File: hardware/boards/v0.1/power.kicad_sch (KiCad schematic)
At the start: 72 parts, among them IC3 SP3401-02UTG, J2 USB, U20 TPS62A02ADRLR, U23 FUSB302BxxMPX, U30 NTJD4401NT1G, U36 STM6601GU2BDM6F, U39 BQ27531YZFR-G1, U45 BQ24193

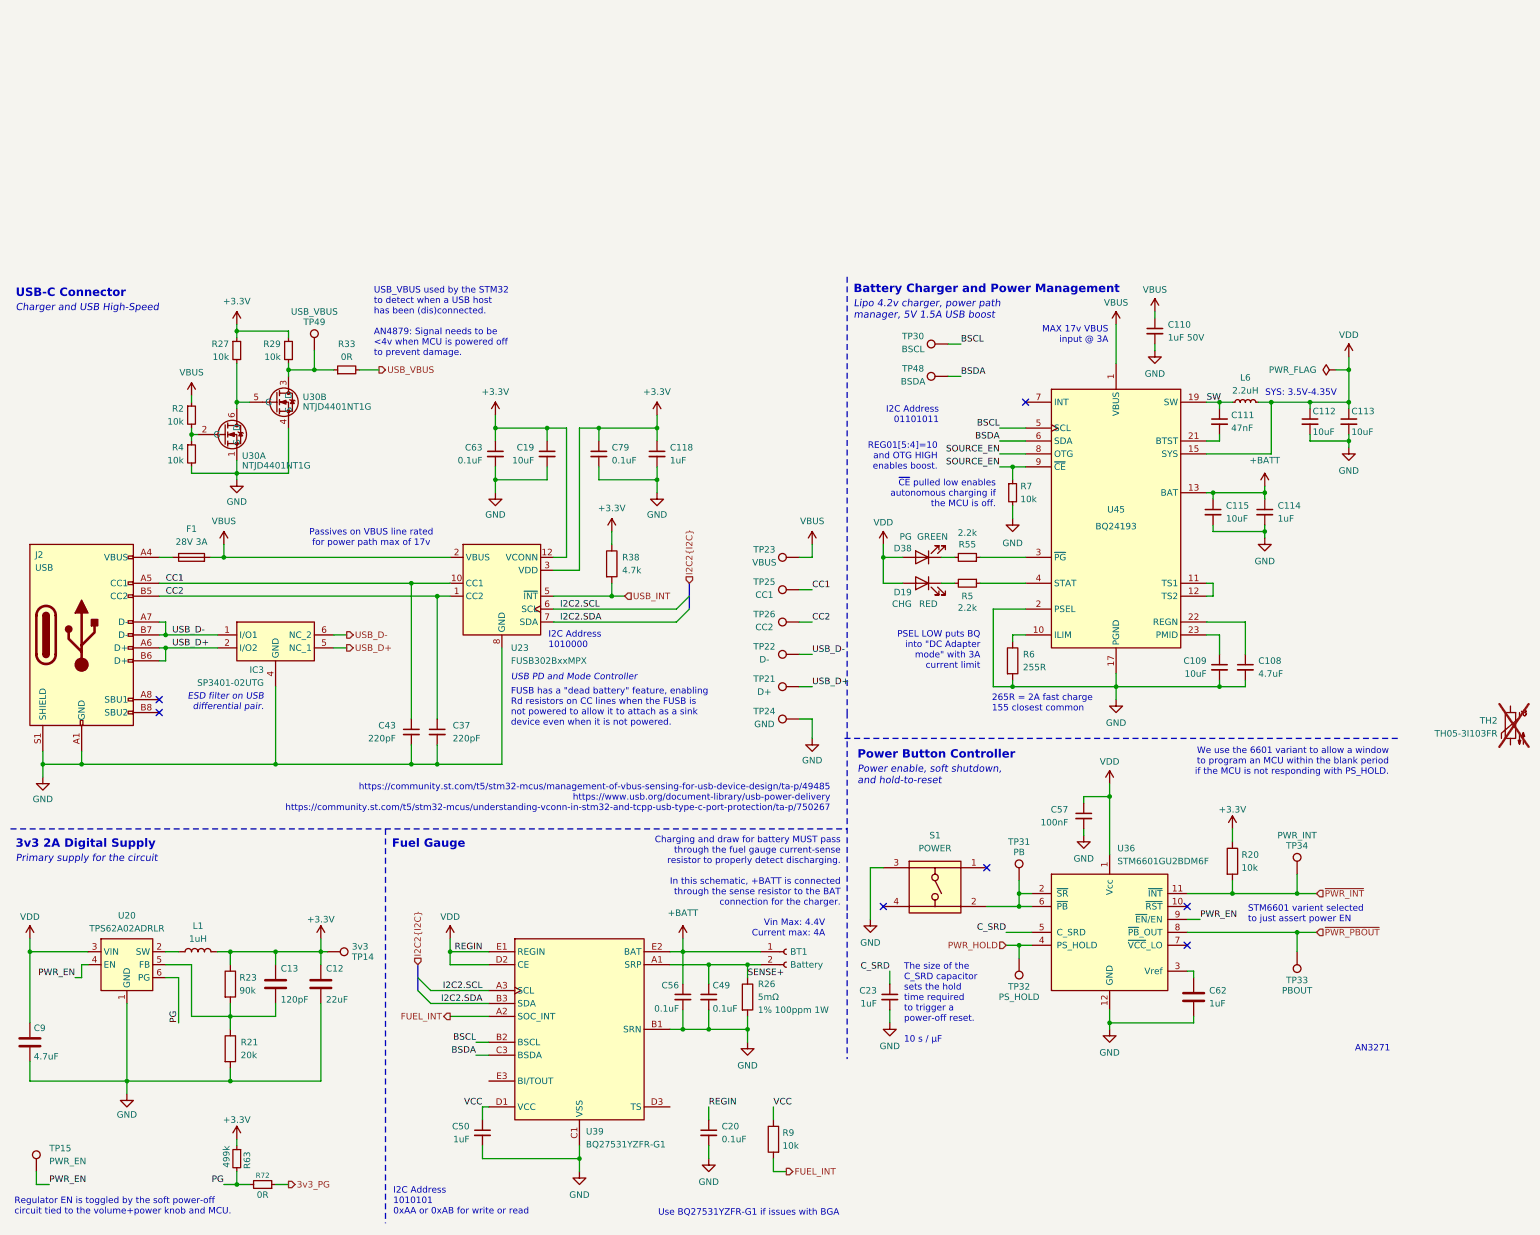
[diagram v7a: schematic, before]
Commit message: feat: various layout and routing adjustments
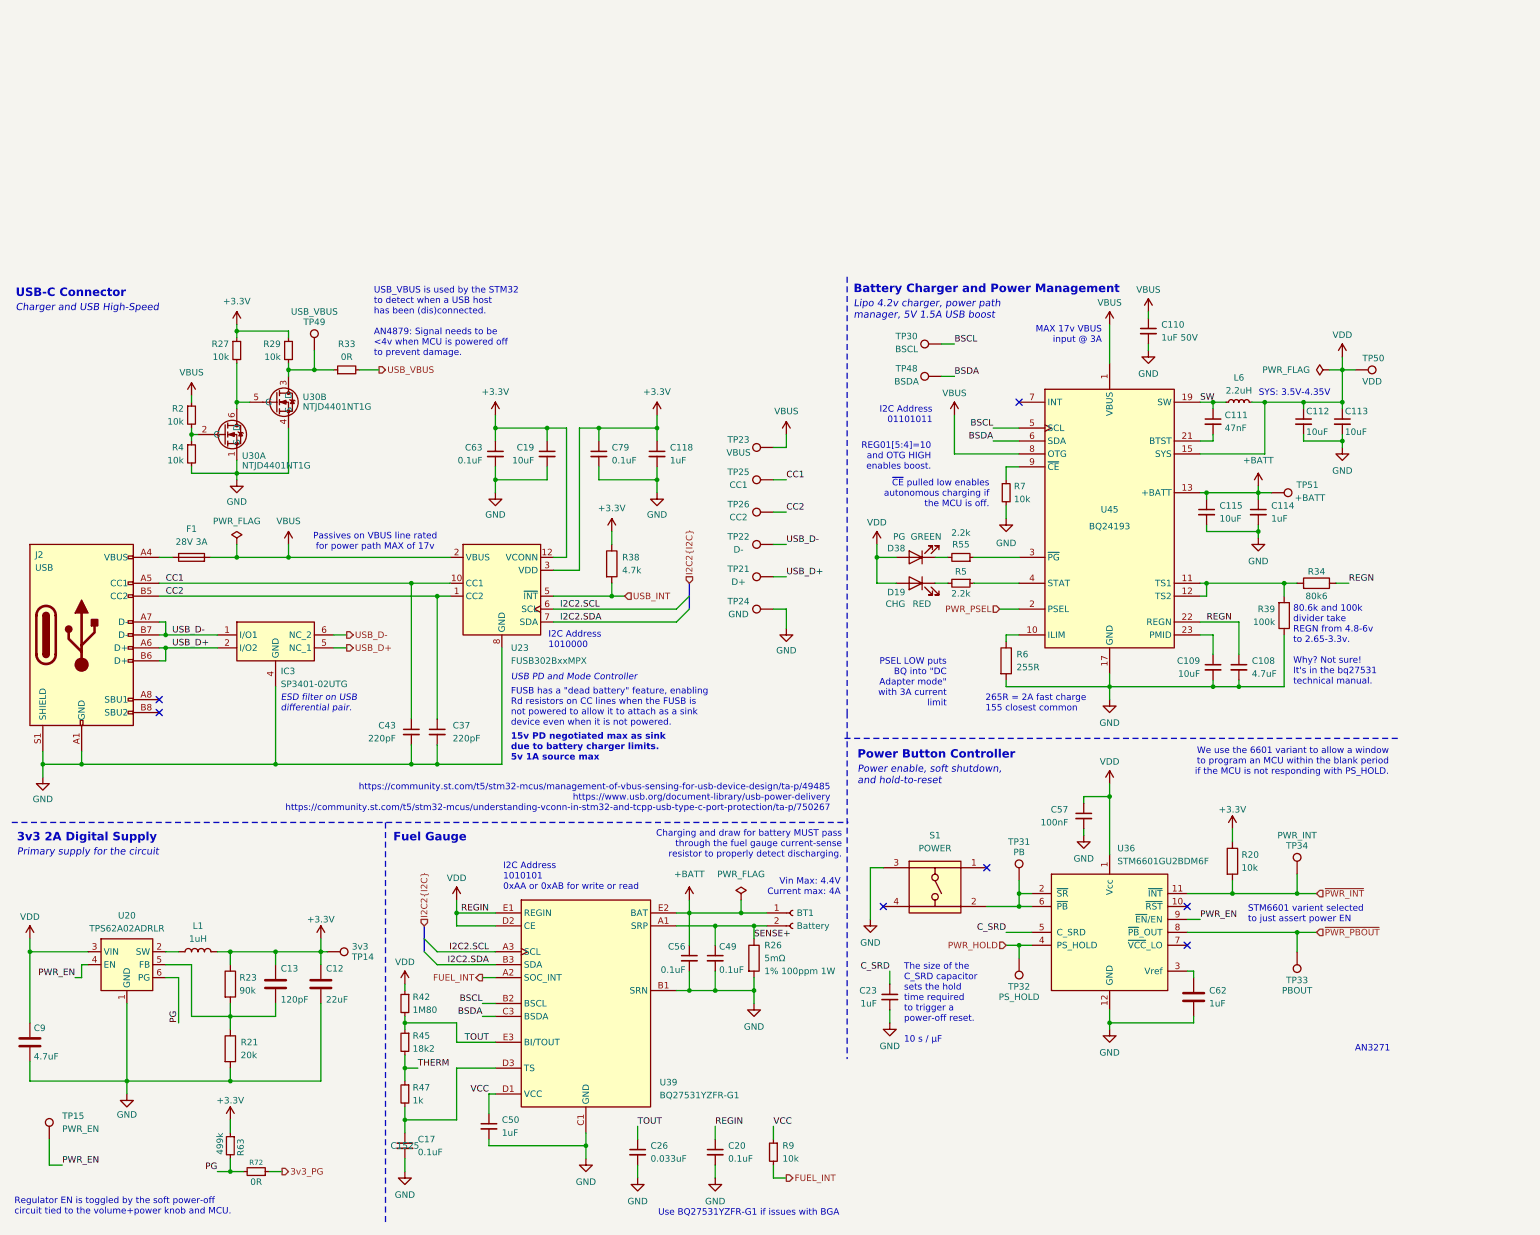
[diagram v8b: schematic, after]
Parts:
- removed TH2: TH05-3I103FR, Resistor_SMD:R_0402_1005Metric_Pad0.72x0.64mm_HandSolder, symbol Device:Thermistor_NTC
- added C17: 0.1uF, Capacitor_SMD:C_0402_1005Metric, symbol Device:C_Small
- added C26: 0.033uF, Capacitor_SMD:C_0402_1005Metric, symbol Device:C_Small
- added R34: 80k6, Resistor_SMD:R_0402_1005Metric, symbol Device:R
- added R39: 100k, Resistor_SMD:R_0402_1005Metric, symbol Device:R
- added R42: 1M80, Resistor_SMD:R_0402_1005Metric, symbol Device:R_Small
- added R45: 18k2, Resistor_SMD:R_0402_1005Metric, symbol Device:R_Small
- added R47: 1k, Resistor_SMD:R_0402_1005Metric, symbol Device:R_Small
- added TP50: VDD, TestPoint:TestPoint_Pad_D1.0mm, symbol Connector:TestPoint
- added TP51: +BATT, TestPoint:TestPoint_Pad_D1.0mm, symbol Connector:TestPoint
- added unit 2 of U30
- R33: JLC (none) -> C17168
- R9: symbol Device:R -> Device:R_Small
- U30: JLC (none) -> C2923388
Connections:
- net +BATT: now also TP51.1
- net GND: now also C17.2, C26.2, R39.1, U30.4 (S); no longer U30.4 (S), U45.2 (PSEL)
- net SYS: now also R42.1, TP50.1
- net VBUS: now also U45.8 (OTG)
- net at U45.11 (TS1), U45.12 (TS2): now also R34.2, R39.2
- net REGN: now reaches C108.1, U45.22 (REGN)
- net REGN: now also R34.1
- net at R29.2, R33.1, TP49.1: now also U30.3 (D); no longer U30.3 (D)
- net at R27.2, U30.6 (D): now also U30.5 (G); no longer U30.5 (G)
- net at U39.D3 (TS): now also C17.1, R47.2
- net TOUT: now reaches U39.E3 (BI/TOUT)
- net TOUT: now also C26.1, R42.2, R45.1
- net SOURCE_EN: no longer names the net of R7.1, U45.9 (~{CE})
- net SOURCE_EN: no longer U45.8 (OTG)
- new net PWR_PSEL: U45.2 (PSEL)
- new net THERM: R45.2, R47.1
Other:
- note added: "15v PD negotiated max as sink due to battery charger limits. 5v 1A source max"
- note added: "80.6k and 100k divider take REGN from 4.8-6v to 2.65-3.3v. Why? Not sure! It's in the bq27531 technical manual."
- note added: "Charging and draw for battery MUST pass through the fuel gauge current-sense resistor to properly detect discharging."
- note added: "Passives on VBUS line rated for power path MAX of 17v"
- note added: "USB_VBUS is used by the STM32 to detect when a USB host has been (dis)connected. AN4879: Signal needs to be <4v when MCU is powered off to prevent damage."
- note removed: "Charging and draw for battery MUST pass through the fuel gauge current-sense resistor to properly detect discharging. In this schematic, +BATT is connected through the sense resistor to the BAT connection for the charger."
- note removed: "Passives on VBUS line rated for power path max of 17v"
- note removed: "USB_VBUS used by the STM32 to detect when a USB host has been (dis)connected. AN4879: Signal needs to be <4v when MCU is powered off to prevent damage."
- moved on the sheet: BT1, C108, C109, C110, C111, C112, C113, C114, C115, C20, C49, C50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
